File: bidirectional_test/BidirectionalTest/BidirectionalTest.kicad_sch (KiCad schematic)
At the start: 0 parts

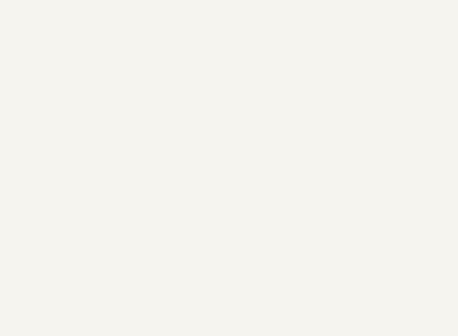
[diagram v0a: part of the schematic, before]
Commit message: fix: Remove 'pass' statements when syncing components from KiCad
When syncing from KiCad to Python, 'pass' statements were being preserved
as user content, causing components to be inserted after 'pass' instead of
replacing it.

Changes:
- Added filter in merge_preserving_user_content() to remove standalone 'pass'
- Only removes 'pass' when generated code has actual components
- Preserves 'pass' when there are no components (keeps valid syntax)

Test case:
- Start with blank circuit (just 'pass')
- Add R1 in KiCad
- Run kicad-to-python
- Result: 'pass' removed, component properly placed

🤖 Generated with [Claude Code](https://claude.com/claude-code)

Co-Authored-By: Claude <noreply@anthropic.com>
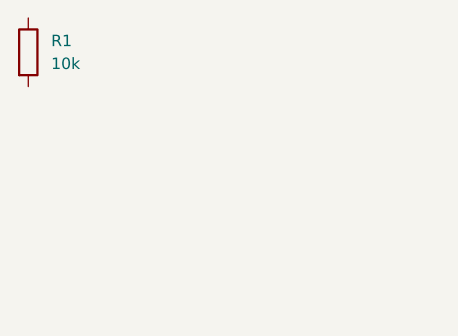
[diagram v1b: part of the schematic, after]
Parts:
- added R1: 10k, Resistor_SMD:R_0603_1608Metric, symbol Device:R
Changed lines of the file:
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@@
 (kicad_sch
 	(version 20250114)
-	(generator "circuit_synth")
-	(generator_version "0.8.36")
+	(generator "eeschema")
+	(generator_version "9.0")
 	(paper "A4")
 	(title_block
@@
 		(margins 1 1 1 1)
 		(stroke
-			(width 0.0000)
+			(width 0)
 			(type solid)
 		)
@@
 		)
 	)
+	(symbol
+		(lib_id "Device:R")
+		(at 101.6 57.15 0)
+		(unit 1)
+		(exclude_from_sim no)
+		(in_bom yes)
+		(on_board yes)
+		(dnp no)
+		(fields_autoplaced yes)
+		(property "Reference" "R1"
+			(at 104.14 55.8799 0)
+			(effects
+				(font
+					(size 1.27 1.27)
+				)
+				(justify left)
+			)
+		)
+		(property "Value" "10k"
+			(at 104.14 58.4199 0)
+			(effects
+				(font
+					(size 1.27 1.27)
+				)
+				(justify left)
+			)
+		)
+		(property "Footprint" "Resistor_SMD:R_0603_1608Metric"
+			(at 99.822 57.15 90)
+			(effects
+				(font
+					(size 1.27 1.27)
+				)
+				(hide yes)
+			)
+		)
+		(property "Datasheet" "~"
+			(at 101.6 57.15 0)
+			(effects
+				(font
+					(size 1.27 1.27)
+				)
+				(hide yes)
+			)
+		)
+		(property "Description" "Resistor"
+			(at 101.6 57.15 0)
+			(effects
+				(font
+					(size 1.27 1.27)
+				)
+				(hide yes)
+			)
+		)
+		(pin "1"
+		)
+		(pin "2"
+		)
+		(instances
+			(project "BidirectionalTest"
+				(path "/fa00019f-a328-4dd4-aa75-20b935f97a3a"
+					(reference "R1")
+					(unit 1)
+				)
+			)
+		)
+	)

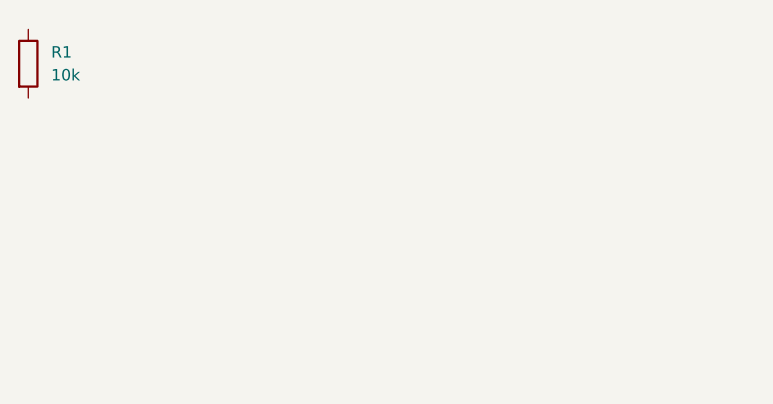
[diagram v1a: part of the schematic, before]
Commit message: test: Verify both directions of bidirectional sync
Manual testing confirms both sync directions working:

1. KiCad → Python:
   - Added R2 in KiCad schematic
   - Ran kicad-to-python BidirectionalTest main.py
   - R2 appeared in Python code ✓

2. Python → KiCad:
   - Added R3 in Python code
   - Ran uv run main.py
   - R3 appeared in KiCad schematic with auto-placement ✓

Both directions verified working with no duplication or data loss.

🤖 Generated with [Claude Code](https://claude.com/claude-code)

Co-Authored-By: Claude <noreply@anthropic.com>
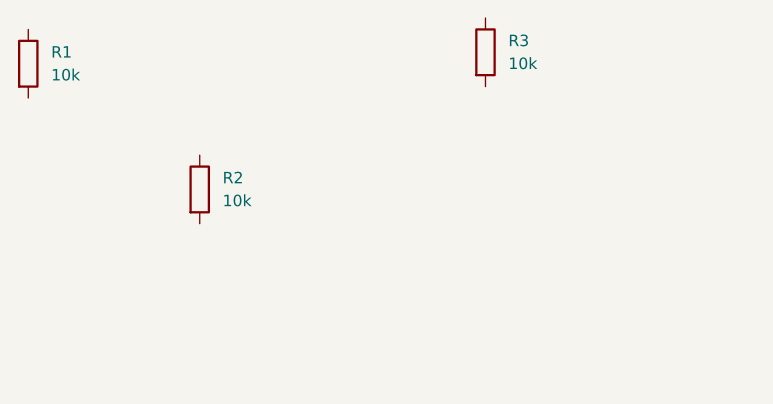
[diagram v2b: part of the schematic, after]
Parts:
- added R2, R3: 10k, Resistor_SMD:R_0603_1608Metric, symbol Device:R
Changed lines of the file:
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@@
 		(title "BidirectionalTest")
-	)
-	(text_box "Bidirectional sync test circuit"
-		(exclude_from_sim no)
-		(at 184 110 0)
-		(size 80 30)
-		(margins 1 1 1 1)
-		(stroke
-			(width 0)
-			(type solid)
-		)
-		(fill
-			(type none)
-		)
-		(effects
-			(font
-				(size 1.2 1.2)
-			)
-			(justify left top)
-		)
 	)
 	(symbol
@@
 			)
 		)
-		(pin "1"
-		)
-		(pin "2"
-		)
 		(instances
-			(project "BidirectionalTest"
+			(project "simple_circuit"
 				(path "/fa00019f-a328-4dd4-aa75-20b935f97a3a"
 					(reference "R1")
@@
 		)
 	)
+	(symbol
+		(lib_id "Device:R")
+		(at 120.65 71.12 0)
+		(unit 1)
+		(exclude_from_sim no)
+		(in_bom yes)
+		(on_board yes)
+		(dnp no)
+		(fields_autoplaced yes)
+		(property "Reference" "R2"
+			(at 123.19 69.8499 0)
+			(effects
+				(font
+					(size 1.27 1.27)
+				)
+				(justify left)
+			)
+		)
+		(property "Value" "10k"
+			(at 123.19 72.3899 0)
+			(effects
+				(font
+					(size 1.27 1.27)
+				)
+				(justify left)
+			)
+		)
+		(property "Footprint" "Resistor_SMD:R_0603_1608Metric"
+			(at 118.872 71.12 90)
+			(effects
+				(font
+					(size 1.27 1.27)
+				)
+				(hide yes)
+			)
+		)
+		(property "Datasheet" "~"
+			(at 120.65 71.12 0)
+			(effects
+				(font
+					(size 1.27 1.27)
+				)
+				(hide yes)
+			)
+		)
+		(property "Description" "Resistor"
+			(at 120.65 71.12 0)
+			(effects
+				(font
+					(size 1.27 1.27)
+				)
+				(hide yes)
+			)
+		)
+		(instances
+			(project "simple_circuit"
+				(path "/fa00019f-a328-4dd4-aa75-20b935f97a3a"
+					(reference "R2")
+					(unit 1)
+				)
+			)
+		)
+	)
+	(symbol
+		(lib_id "Device:R")
+		(at 152.4 55.88 0)
+		(unit 1)
+		(exclude_from_sim no)
+		(in_bom yes)
+		(on_board yes)
+		(dnp no)
+		(fields_autoplaced yes)
+		(property "Reference" "R3"
+			(at 154.94 54.6099 0)
+			(effects
+				(font
+					(size 1.27 1.27)
+				)
+				(justify left)
+			)
+		)
+		(property "Value" "10k"
+			(at 154.94 57.1499 0)
+			(effects
+				(font
+					(size 1.27 1.27)
+				)
+				(justify left)
+			)
+		)
+		(property "Footprint" "Resistor_SMD:R_0603_1608Metric"
+			(at 150.622 55.88 90)
+			(effects
+				(font
+					(size 1.27 1.27)
+				)
+				(hide yes)
+			)
+		)
+		(pin "1"
+		)
+		(pin "2"
+		)
+		(instances
+			(project "simple_circuit"
+				(path "/fa00019f-a328-4dd4-aa75-20b935f97a3a"
+					(reference "R3")
+					(unit 1)
+				)
+			)
+		)
+	)
+	(text_box "Bidirectional sync test circuit"
+		(exclude_from_sim no)
+		(at 184 110 0.0000)
+		(size 80 30)
+		(margins 1 1 1 1)
+		(stroke
+			(width 0.0000)
+			(type solid)
+		)
+		(fill
+			(type none)
+		)
+		(effects
+			(font
+				(size 1.2 1.2)
+			)
+			(justify left top)
+		)
+	)

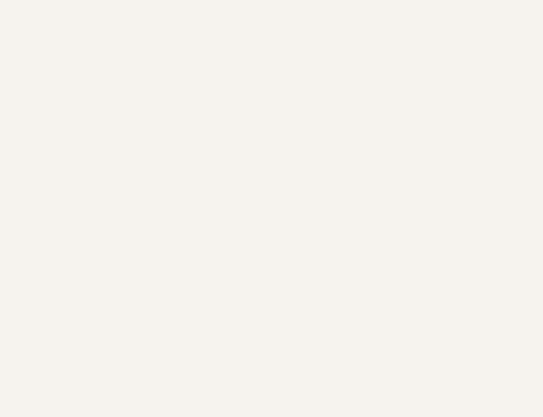
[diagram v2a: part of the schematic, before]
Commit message: docs: Document hierarchical schematic limitation
Manual testing revealed that hierarchical schematics (sheet symbols) are
not currently supported in bidirectional sync.

Test Case:
- Added sheet symbol to KiCad project (shane1.kicad_sch)
- Ran kicad-to-python BidirectionalTest main.py
- Parser warnings: 'Could not parse sheet block: name=None, file=None'
- No separate Python file created for the sheet

Expected Behavior:
- Should detect sheet from main schematic
- Create shane1.py with subcircuit definition
- Update main.py to import and instantiate shane1

Current Behavior:
- Sheets are ignored
- Only root schematic components synced
- No hierarchical structure in Python code

This is a significant feature gap that needs to be addressed in a
future PR. For now, users should use flat (non-hierarchical) schematics.

🤖 Generated with [Claude Code](https://claude.com/claude-code)

Co-Authored-By: Claude <noreply@anthropic.com>
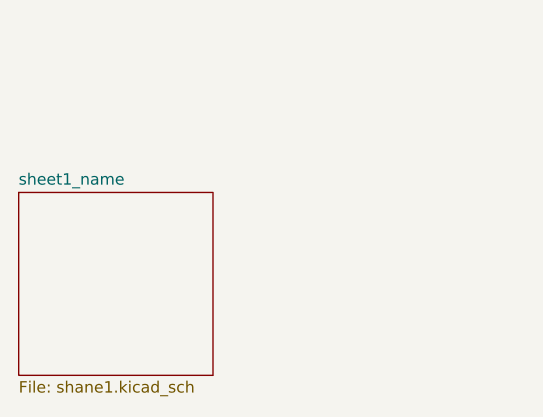
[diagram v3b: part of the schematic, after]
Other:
- added sheet sheet1_name (shane1.kicad_sch)
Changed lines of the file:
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@@
 		(title "BidirectionalTest")
+	)
+	(text_box "Bidirectional sync test circuit"
+		(exclude_from_sim no)
+		(at 184 110 0)
+		(size 80 30)
+		(margins 1 1 1 1)
+		(stroke
+			(width 0)
+			(type solid)
+		)
+		(fill
+			(type none)
+		)
+		(effects
+			(font
+				(size 1.2 1.2)
+			)
+			(justify left top)
+		)
 	)
 	(symbol
@@
 			)
 		)
+		(pin "1"
+		)
+		(pin "2"
+		)
 		(instances
 			(project "simple_circuit"
@@
 			)
 		)
+		(pin "1"
+		)
+		(pin "2"
+		)
 		(instances
 			(project "simple_circuit"
@@
 			)
 		)
+		(property "Datasheet" ""
+			(at 152.4 55.88 0)
+			(effects
+				(font
+					(size 1.27 1.27)
+				)
+			)
+		)
+		(property "Description" ""
+			(at 152.4 55.88 0)
+			(effects
+				(font
+					(size 1.27 1.27)
+				)
+			)
+		)
 		(pin "1"
 		)
@@
 		)
 	)
-	(text_box "Bidirectional sync test circuit"
-		(exclude_from_sim no)
-		(at 184 110 0.0000)
-		(size 80 30)
-		(margins 1 1 1 1)
+	(sheet
+		(at 91.44 118.11)
+		(size 21.59 20.32)
+		(exclude_from_sim no)
+		(in_bom yes)
+		(on_board yes)
+		(dnp no)
+		(fields_autoplaced yes)
 		(stroke
-			(width 0.0000)
+			(width 0.1524)
 			(type solid)
 		)
 		(fill
-			(type none)
-		)
-		(effects
-			(font
-				(size 1.2 1.2)
-			)
-			(justify left top)
-		)
-	)
+			(color 0 0 0 0.0000)
+		)
+		(property "Sheetname" "sheet1_name"
+			(at 91.44 117.3984 0)
+			(effects
+				(font
+					(size 1.27 1.27)
+				)
+				(justify left bottom)
+			)
+		)
+		(property "Sheetfile" "shane1.kicad_sch"
+			(at 91.44 139.0146 0)
+			(effects
+				(font
+					(size 1.27 1.27)
+				)
+				(justify left top)
+			)
+		)
+		(instances
+			(project "BidirectionalTest"
+				(path "/fa00019f-a328-4dd4-aa75-20b935f97a3a"
+					(page "2")
+				)
+			)
+		)
+	)
